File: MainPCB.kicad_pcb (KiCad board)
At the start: 6 copper layers, 128 x 89.5 mm, 108 parts, among them IC1 VNH7070ASTR, IC2 VNH7070ASTR, IC3 VNH7070ASTR, IC4 VNH7070ASTR, IC5 VNH7070ASTR, J1 Conn_01x06, J10 Conn_01x02, J101 TYPEC-305-ACP16H458, J11 Conn_01x03, J2 Conn_01x03, J20 Conn_01x02_Pin, J3 Conn_01x03_Pin, J4 Conn_01x02, J5 Screw_Terminal_01x02, J501 GT-HD001B-CNNG1, J6 Conn_01x04_Pin, J7 Conn_01x04_Pin, J8 Conn_01x02, J802 Conn_01x22_Female, J9 Conn_01x06_Pin, M1 Motor_DC, M2 Motor_DC, M3 Motor_DC, M4 Motor_DC, M5 Motor_DC, SW1 SW_DPST_x2, SW2 SW_DPST_x2, U1 MagJack-A70-112-331N126, U10 N channel, U12 Teensy4.1, U21 V_Regulator3.3v, U22 V_Regulator5v, U4 BNO055, U401 TPD4EUSB30, U402 TPD4EUSB30, U405 STMPS2151STR, U602 SN74LVC1G14DBVR, U701 AP22653W6

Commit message: Fixed Outline and moved around holes
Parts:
- moved H1 23.1 mm to (151.7, 128.3)
- moved H2 11.5 mm to (59.5, 124.5)
- moved R19 3.61 mm to (141.4, 152.4)
- moved SW2 2.24 mm to (144.8, 144.1)
- moved J11 1.49 mm to (137.5, 143.3)
- moved SW1 0.97 mm to (145.7, 133.0)
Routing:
- net Net-(J5-Pin_2): track 37.1 -> 39.4 mm
- net Start/Stop: track 111.8 -> 113.9 mm
- net PWM-LIDAR: track 119.6 -> 121.3 mm
- net 12V: track 319.9 -> 319.2 mm
- net LightGate: track 114.3 -> 115.0 mm
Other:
- outline, holes or cut-outs redrawn

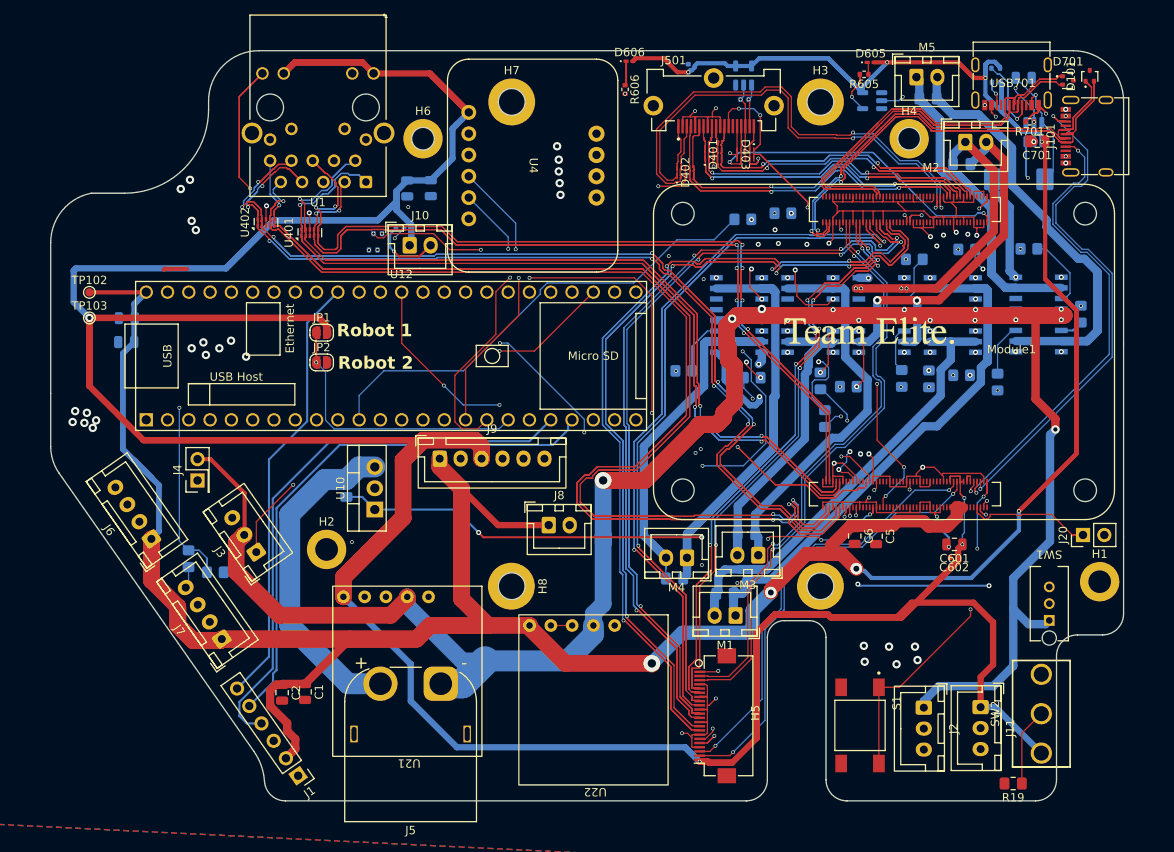
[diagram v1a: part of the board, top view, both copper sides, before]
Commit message: fixed drc errors
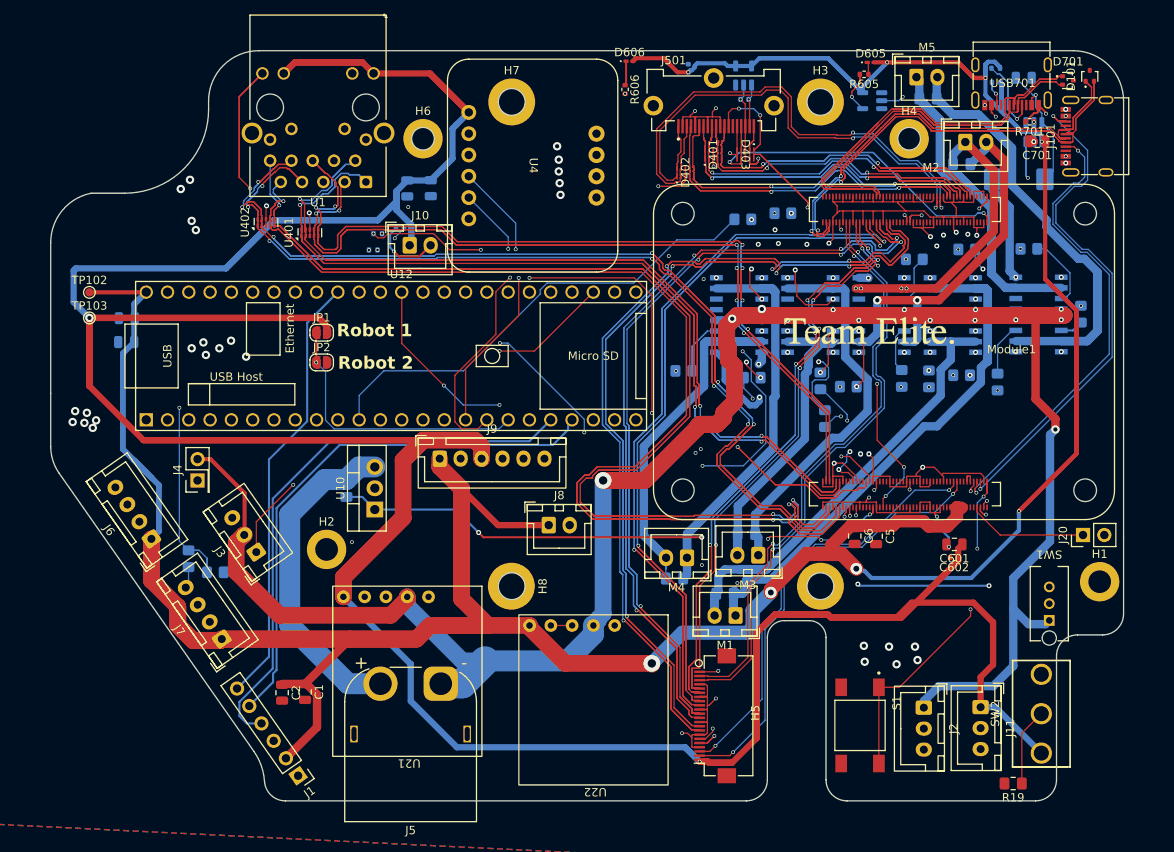
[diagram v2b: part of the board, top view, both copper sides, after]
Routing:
- net 3.3V: track 539.0 -> 524.8 mm, vias 4 -> 2
- net Net-(U701-ILIM): track 6.55 -> 0.06 mm, vias 2 -> 1
- net Net-(IC4-OUT_A_1): track 71.1 -> 65.0 mm
- net 5V: track 501.8 -> 498.5 mm
- net 12V: track 319.2 -> 316.8 mm
- net /CM5/nRPIBOOT: track 16.4 -> 14.3 mm
- net Net-(SW1A-B): track 90.5 -> 89.8 mm
- net GND: track 237.5 -> 236.8 mm
